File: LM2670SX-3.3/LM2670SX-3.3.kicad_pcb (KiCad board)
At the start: 2 copper layers, 19.6 x 32.4 mm, 10 parts, among them IC1 LM2670SX-3.3_NOPB, J1 Conn_01x03

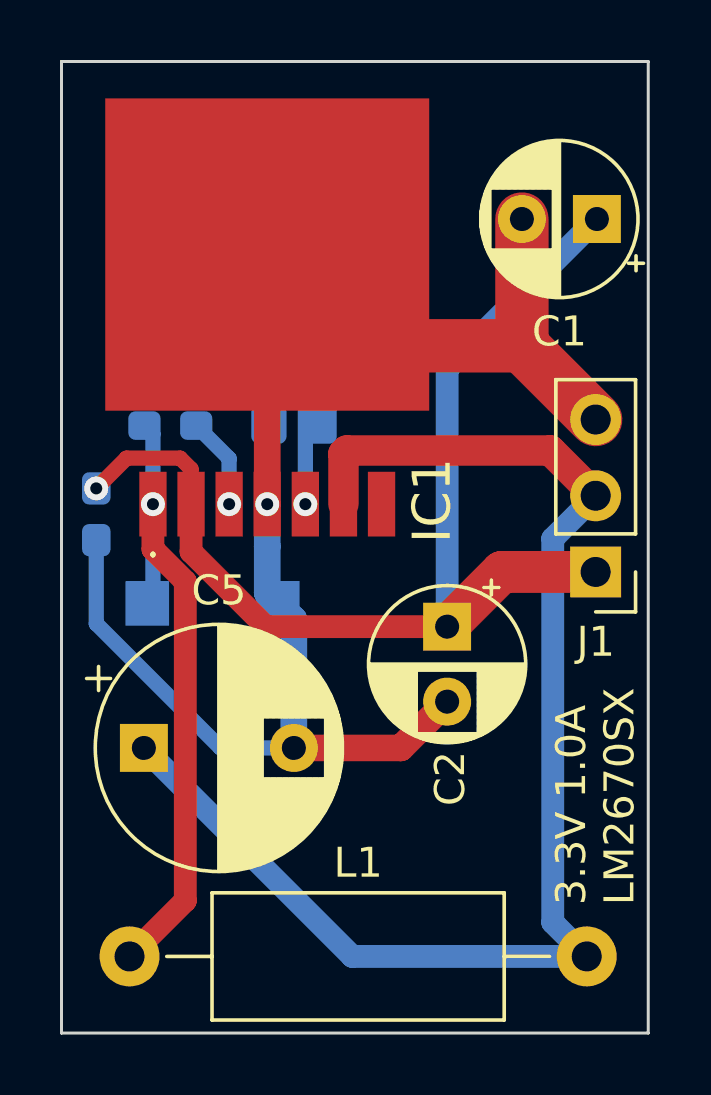
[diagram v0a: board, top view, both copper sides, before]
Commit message: fixing some routes and DRC'ed it.
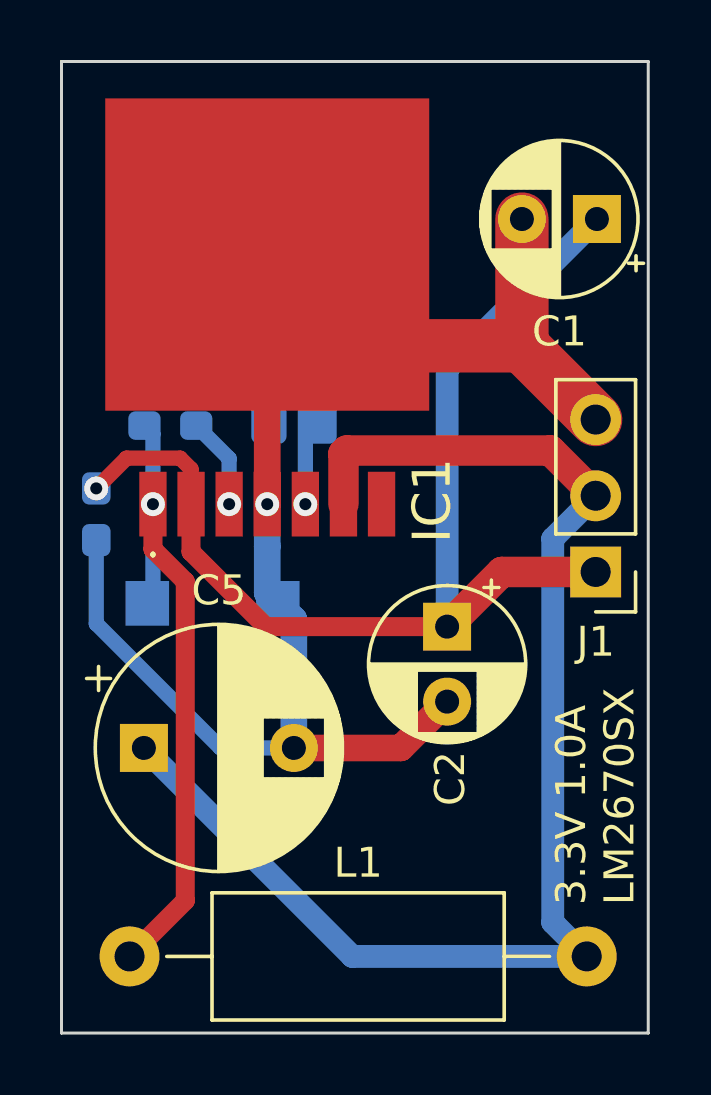
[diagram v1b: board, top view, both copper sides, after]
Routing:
- net GND: track 54.8 -> 50.5 mm
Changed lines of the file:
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@@
     (effects (font (size 1 1) (thickness 0.15)) (justify left bottom))
   )
-  (segment (start 175.26 100.798) (end 177.755055 103.293055) (width 0.762) (layer "F.Cu") (net 1))
-  (segment (start 185.619369 101.4702) (end 183.796514 103.293055) (width 1.397) (layer "F.Cu") (net 1))
+  (segment (start 175.26 100.798) (end 177.755055 103.293055) (width 0.635) (layer "F.Cu") (net 1))
+  (segment (start 185.619369 101.4702) (end 183.796514 103.293055) (width 1.016) (layer "F.Cu") (net 1))
   (segment (start 174.899 97.676) (end 173.109789 97.676) (width 0.508) (layer "F.Cu") (net 1))
-  (segment (start 188.7477 101.4702) (end 185.619369 101.4702) (width 1.397) (layer "F.Cu") (net 1))
-  (segment (start 175.26 99.21) (end 175.26 100.798) (width 0.762) (layer "F.Cu") (net 1))
-  (segment (start 177.755055 103.293055) (end 183.796514 103.293055) (width 0.762) (layer "F.Cu") (net 1))
+  (segment (start 188.7477 101.4702) (end 185.619369 101.4702) (width 1.016) (layer "F.Cu") (net 1))
+  (segment (start 175.26 99.21) (end 175.26 100.798) (width 0.635) (layer "F.Cu") (net 1))
+  (segment (start 177.755055 103.293055) (end 183.796514 103.293055) (width 0.635) (layer "F.Cu") (net 1))
   (segment (start 175.26 99.21) (end 175.26 98.037) (width 0.508) (layer "F.Cu") (net 1))
   (segment (start 175.26 98.037) (end 174.899 97.676) (width 0.508) (layer "F.Cu") (net 1))
@@
   (segment (start 178.687637 107.336169) (end 182.2534 107.336169) (width 0.889) (layer "F.Cu") (net 2))
   (segment (start 182.2534 107.336169) (end 183.796514 105.793055) (width 0.889) (layer "F.Cu") (net 2))
-  (segment (start 180.841445 93.931445) (end 177.8 90.89) (width 1.778) (layer "F.Cu") (net 2))
   (segment (start 186.288945 93.931445) (end 180.841445 93.931445) (width 1.778) (layer "F.Cu") (net 2))
   (segment (start 186.288945 93.931445) (end 188.7477 96.3902) (width 1.778) (layer "F.Cu") (net 2))
@@
   (segment (start 176.53 97.688276) (end 175.43204 96.590316) (width 0.508) (layer "B.Cu") (net 3))
   (segment (start 176.53 99.21) (end 176.53 97.688276) (width 0.508) (layer "B.Cu") (net 3))
-  (segment (start 175.068637 101.787505) (end 173.99 100.708868) (width 0.762) (layer "F.Cu") (net 4))
-  (segment (start 173.209934 114.285576) (end 175.068637 112.426873) (width 0.762) (layer "F.Cu") (net 4))
-  (segment (start 173.99 100.708868) (end 173.99 99.21) (width 0.762) (layer "F.Cu") (net 4))
-  (segment (start 175.068637 112.426873) (end 175.068637 101.787505) (width 0.762) (layer "F.Cu") (net 4))
+  (segment (start 175.068637 101.787505) (end 173.99 100.708868) (width 0.635) (layer "F.Cu") (net 4))
+  (segment (start 173.209934 114.285576) (end 175.068637 112.426873) (width 0.635) (layer "F.Cu") (net 4))
+  (segment (start 173.99 100.708868) (end 173.99 99.21) (width 0.635) (layer "F.Cu") (net 4))
+  (segment (start 175.068637 112.426873) (end 175.068637 101.787505) (width 0.635) (layer "F.Cu") (net 4))
   (via (at 173.99 99.21) (size 0.8) (drill 0.4) (layers "F.Cu" "B.Cu") (free) (net 4))
-  (segment (start 173.99 102.330114) (end 173.80243 102.517684) (width 0.508) (layer "B.Cu") (net 4))
   (segment (start 173.99 96.873276) (end 173.70704 96.590316) (width 0.508) (layer "B.Cu") (net 4))
   (segment (start 173.99 99.21) (end 173.99 102.330114) (width 0.508) (layer "B.Cu") (net 4))
